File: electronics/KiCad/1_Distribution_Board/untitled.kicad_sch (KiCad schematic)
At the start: 5 parts, among them J301 Conn_01x02, J302 Conn_01x02

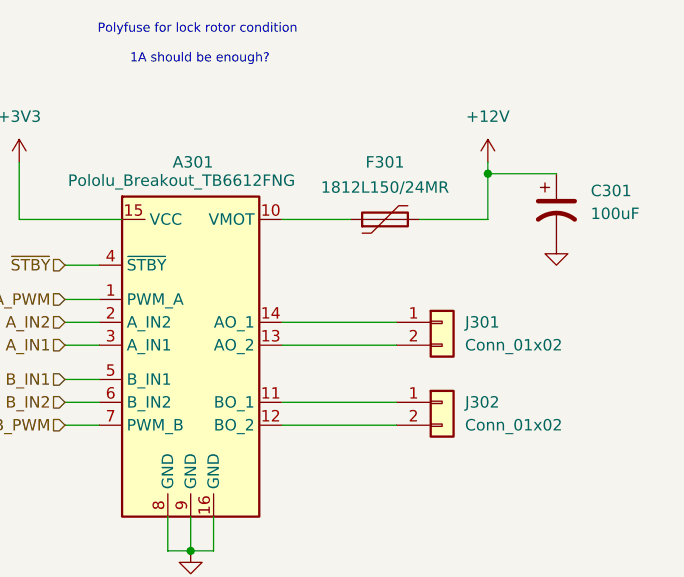
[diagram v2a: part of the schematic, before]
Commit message: Added 4th stepper
Added 4th stepper on SCH and PCB
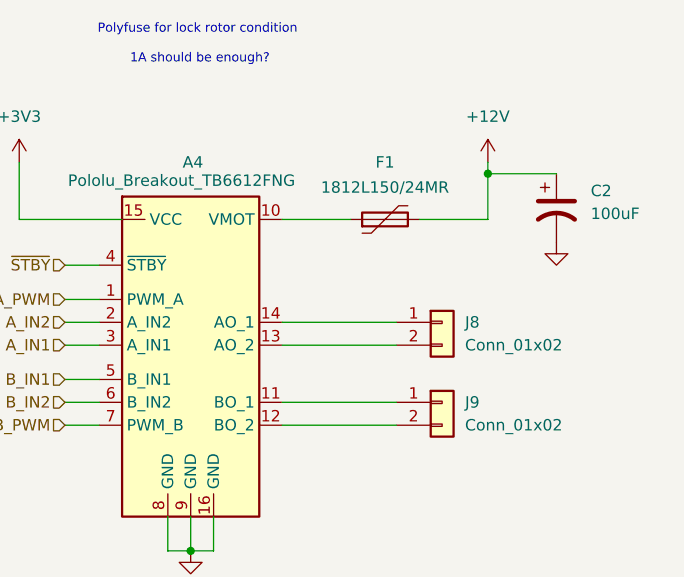
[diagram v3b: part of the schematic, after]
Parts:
- renumbered A301 to A4, C301 to C2, F301 to F1, J301 to J8, J302 to J9
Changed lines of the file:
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@@
 		(dnp no)
 		(fields_autoplaced yes)
-		(property "Reference" "J301"
+		(property "Reference" "J8"
 			(at 167.64 95.2499 0)
 			(effects
@@
 			(project "1_Distribution_Board"
 				(path "/d53c8c01-e754-4310-8a73-7d7c95e64cd3/406ed9e9-c014-4ad1-b5c7-3c59cc994d52"
-					(reference "J401")
-					(unit 1)
-				)
-				(path "/d53c8c01-e754-4310-8a73-7d7c95e64cd3/6afb3c5f-c712-4230-bfac-30dcc87f4845"
-					(reference "J301")
+					(reference "J10")
+					(unit 1)
+				)
+				(path "/d53c8c01-e754-4310-8a73-7d7c95e64cd3/6afb3c5f-c712-4230-bfac-30dcc87f4845"
+					(reference "J8")
 					(unit 1)
 				)
@@
 		(on_board yes)
 		(dnp no)
-		(property "Reference" "A301"
+		(property "Reference" "A4"
 			(at 137.414 77.47 0)
 			(effects
@@
 			(project "1_Distribution_Board"
 				(path "/d53c8c01-e754-4310-8a73-7d7c95e64cd3/406ed9e9-c014-4ad1-b5c7-3c59cc994d52"
-					(reference "A401")
-					(unit 1)
-				)
-				(path "/d53c8c01-e754-4310-8a73-7d7c95e64cd3/6afb3c5f-c712-4230-bfac-30dcc87f4845"
-					(reference "A301")
+					(reference "A5")
+					(unit 1)
+				)
+				(path "/d53c8c01-e754-4310-8a73-7d7c95e64cd3/6afb3c5f-c712-4230-bfac-30dcc87f4845"
+					(reference "A4")
 					(unit 1)
 				)
@@
 		(dnp no)
 		(fields_autoplaced yes)
-		(property "Reference" "#PWR0304"
+		(property "Reference" "#PWR026"
 			(at 137.16 127 0)
 			(effects
@@
 			(project "1_Distribution_Board"
 				(path "/d53c8c01-e754-4310-8a73-7d7c95e64cd3/406ed9e9-c014-4ad1-b5c7-3c59cc994d52"
-					(reference "#PWR0404")
-					(unit 1)
-				)
-				(path "/d53c8c01-e754-4310-8a73-7d7c95e64cd3/6afb3c5f-c712-4230-bfac-30dcc87f4845"
-					(reference "#PWR0304")
+					(reference "#PWR030")
+					(unit 1)
+				)
+				(path "/d53c8c01-e754-4310-8a73-7d7c95e64cd3/6afb3c5f-c712-4230-bfac-30dcc87f4845"
+					(reference "#PWR026")
 					(unit 1)
 				)
@@
 		(dnp no)
 		(fields_autoplaced yes)
-		(property "Reference" "#PWR0301"
+		(property "Reference" "#PWR025"
 			(at 118.11 81.28 0)
 			(effects
@@
 			(project "1_Distribution_Board"
 				(path "/d53c8c01-e754-4310-8a73-7d7c95e64cd3/406ed9e9-c014-4ad1-b5c7-3c59cc994d52"
-					(reference "#PWR0401")
-					(unit 1)
-				)
-				(path "/d53c8c01-e754-4310-8a73-7d7c95e64cd3/6afb3c5f-c712-4230-bfac-30dcc87f4845"
-					(reference "#PWR0301")
+					(reference "#PWR029")
+					(unit 1)
+				)
+				(path "/d53c8c01-e754-4310-8a73-7d7c95e64cd3/6afb3c5f-c712-4230-bfac-30dcc87f4845"
+					(reference "#PWR025")
 					(unit 1)
 				)
@@
 		(dnp no)
 		(fields_autoplaced yes)
-		(property "Reference" "#PWR0302"
+		(property "Reference" "#PWR027"
 			(at 170.18 81.28 0)
 			(effects
@@
 			(project "1_Distribution_Board"
 				(path "/d53c8c01-e754-4310-8a73-7d7c95e64cd3/406ed9e9-c014-4ad1-b5c7-3c59cc994d52"
-					(reference "#PWR0402")
-					(unit 1)
-				)
-				(path "/d53c8c01-e754-4310-8a73-7d7c95e64cd3/6afb3c5f-c712-4230-bfac-30dcc87f4845"
-					(reference "#PWR0302")
+					(reference "#PWR031")
+					(unit 1)
+				)
+				(path "/d53c8c01-e754-4310-8a73-7d7c95e64cd3/6afb3c5f-c712-4230-bfac-30dcc87f4845"
+					(reference "#PWR027")
 					(unit 1)
 				)
@@
 		(dnp no)
 		(fields_autoplaced yes)
-		(property "Reference" "C301"
+		(property "Reference" "C2"
 			(at 181.61 80.6449 0)
 			(effects
@@
 			(project "1_Distribution_Board"
 				(path "/d53c8c01-e754-4310-8a73-7d7c95e64cd3/406ed9e9-c014-4ad1-b5c7-3c59cc994d52"
-					(reference "C401")
-					(unit 1)
-				)
-				(path "/d53c8c01-e754-4310-8a73-7d7c95e64cd3/6afb3c5f-c712-4230-bfac-30dcc87f4845"
-					(reference "C301")
+					(reference "C3")
+					(unit 1)
+				)
+				(path "/d53c8c01-e754-4310-8a73-7d7c95e64cd3/6afb3c5f-c712-4230-bfac-30dcc87f4845"
+					(reference "C2")
 					(unit 1)
 				)
@@
 		(dnp no)
 		(fields_autoplaced yes)
-		(property "Reference" "J302"
+		(property "Reference" "J9"
 			(at 167.64 104.1399 0)
 			(effects
@@
 			(project "1_Distribution_Board"
 				(path "/d53c8c01-e754-4310-8a73-7d7c95e64cd3/406ed9e9-c014-4ad1-b5c7-3c59cc994d52"
-					(reference "J402")
-					(unit 1)
-				)
-				(path "/d53c8c01-e754-4310-8a73-7d7c95e64cd3/6afb3c5f-c712-4230-bfac-30dcc87f4845"
-					(reference "J302")
+					(reference "J11")
+					(unit 1)
+				)
+				(path "/d53c8c01-e754-4310-8a73-7d7c95e64cd3/6afb3c5f-c712-4230-bfac-30dcc87f4845"
+					(reference "J9")
 					(unit 1)
 				)
@@
 		(on_board yes)
 		(dnp no)
-		(property "Reference" "F301"
+		(property "Reference" "F1"
 			(at 158.75 77.47 90)
 			(effects
@@
 			(project "1_Distribution_Board"
 				(path "/d53c8c01-e754-4310-8a73-7d7c95e64cd3/406ed9e9-c014-4ad1-b5c7-3c59cc994d52"
-					(reference "F401")
-					(unit 1)
-				)
-				(path "/d53c8c01-e754-4310-8a73-7d7c95e64cd3/6afb3c5f-c712-4230-bfac-30dcc87f4845"
-					(reference "F301")
+					(reference "F2")
+					(unit 1)
+				)
+				(path "/d53c8c01-e754-4310-8a73-7d7c95e64cd3/6afb3c5f-c712-4230-bfac-30dcc87f4845"
+					(reference "F1")
 					(unit 1)
 				)
@@
 		(dnp no)
 		(fields_autoplaced yes)
-		(property "Reference" "#PWR0303"
+		(property "Reference" "#PWR028"
 			(at 177.8 92.71 0)
 			(effects
@@
 			(project "1_Distribution_Board"
 				(path "/d53c8c01-e754-4310-8a73-7d7c95e64cd3/406ed9e9-c014-4ad1-b5c7-3c59cc994d52"
-					(reference "#PWR0403")
-					(unit 1)
-				)
-				(path "/d53c8c01-e754-4310-8a73-7d7c95e64cd3/6afb3c5f-c712-4230-bfac-30dcc87f4845"
-					(reference "#PWR0303")
-					(unit 1)
-				)
+					(reference "#PWR032")
+					(unit 1)
+				)
+				(path "/d53c8c01-e754-4310-8a73-7d7c95e64cd3/6afb3c5f-c712-4230-bfac-30dcc87f4845"
+					(reference "#PWR028")
+					(unit 1)
+				)
